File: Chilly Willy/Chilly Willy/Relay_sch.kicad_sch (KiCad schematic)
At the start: 0 parts

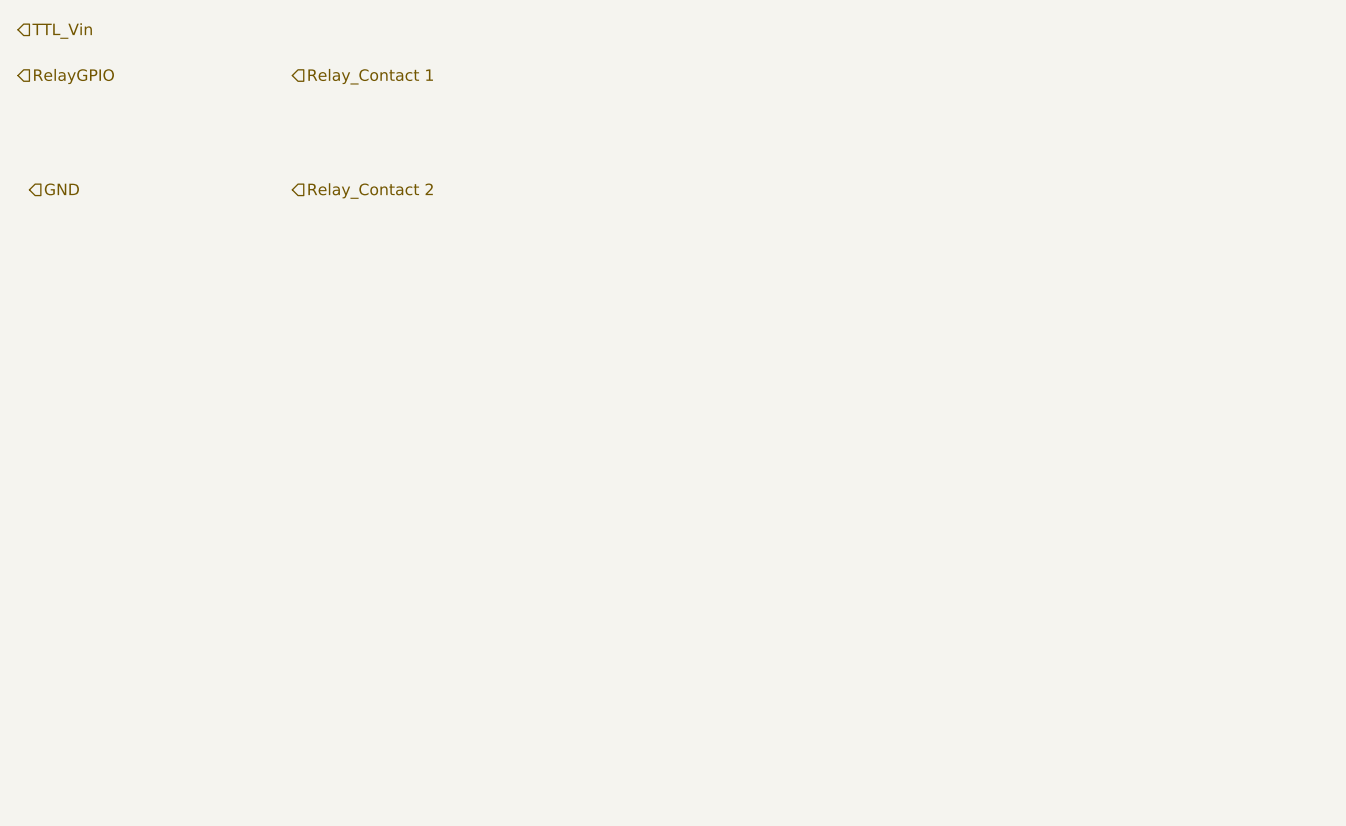
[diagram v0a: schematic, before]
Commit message: * adding in the Relays * GPIO via MCP23008
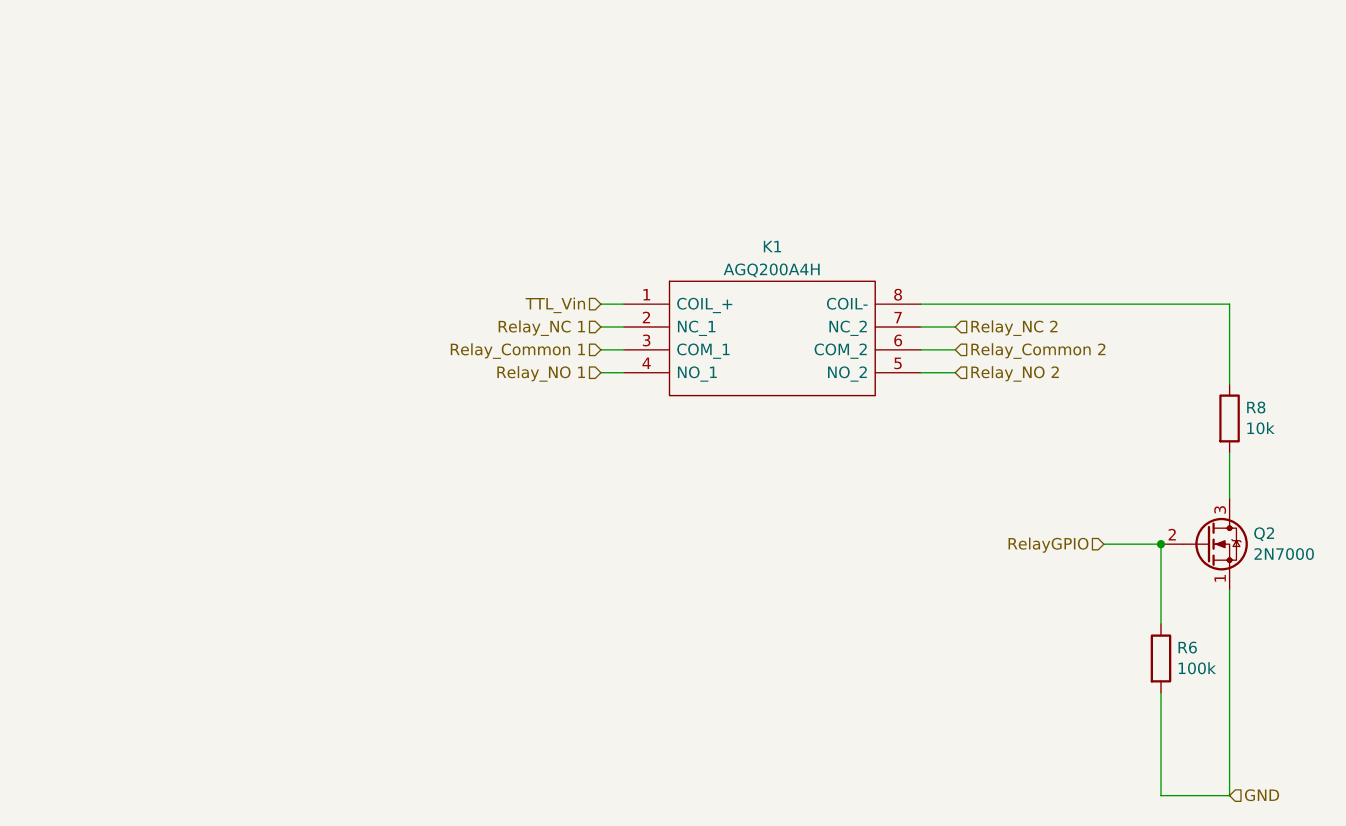
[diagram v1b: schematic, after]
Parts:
- added K1: AGQ200A4H, AGQ200A12, symbol SamacSys_Parts:AGQ200A4H
- added Q2: 2N7000, Package_TO_SOT_THT:TO-92_Inline, symbol Transistor_FET:2N7000
- added R6: 100k, Resistor_THT:R_Axial_DIN0207_L6.3mm_D2.5mm_P2.54mm_Vertical, symbol Device:R
- added R8: 10k, Resistor_THT:R_Axial_DIN0207_L6.3mm_D2.5mm_P2.54mm_Vertical, symbol Device:R
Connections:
- net GND: now also Q2.1 (S), R6.2
- net RelayGPIO: now also Q2.2 (G), R6.1
- net TTL_Vin: now also K1.1 (COIL_+)
- new net: K1.8 (COIL-), R8.1
- new net: Q2.3 (D), R8.2
- new net Relay_Common 1: K1.3 (COM_1)
- new net Relay_Common 2 : K1.6 (COM_2)
- new net Relay_NC 1: K1.2 (NC_1)
- new net Relay_NC 2: K1.7 (NC_2)
- new net Relay_NO 1: K1.4 (NO_1)
- new net Relay_NO 2: K1.5 (NO_2)

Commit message: ..
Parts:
- removed K1: AGQ200A4H, AGQ200A12, symbol SamacSys_Parts:AGQ200A4H
- added K2: G6L-1F-TRDC4.5, G6L1FTRDC45, symbol SamacSys_Parts:G6L-1F-TRDC4.5
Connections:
- net Relay_Common 1: now also K2.2 (COM)
- net Relay_NO 1: now also K2.4 (NO)
- net TTL_Vin: now also K2.8 (COIL_2)
- net at R8.1: now also K2.5 (COIL_1)
